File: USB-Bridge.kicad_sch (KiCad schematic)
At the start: 14 parts, among them J3 USB_B_Micro, Q4 LRC L8050QLT1G, Q5 LRC L8050QLT1G, U2 CP2102N-A02-GQFN24

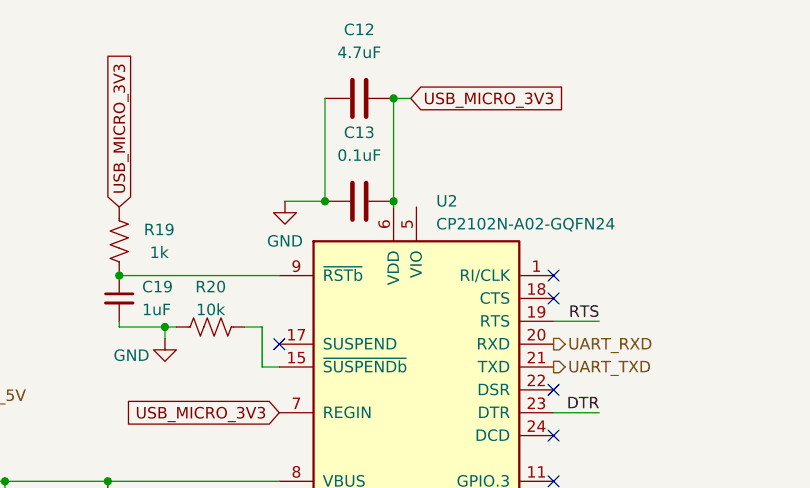
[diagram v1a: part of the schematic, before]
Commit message: added screen and gpio buttons
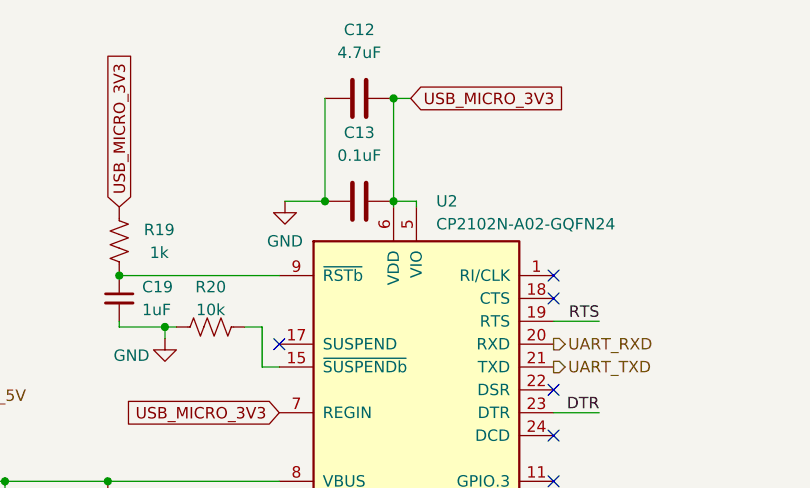
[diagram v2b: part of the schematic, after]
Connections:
- net USB_MICRO_3V3: now also U2.5 (VIO)
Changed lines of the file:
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@@
+	(wire
+		(pts
+			(xy 163.195 56.515) (xy 163.195 57.15)
+		)
+		(stroke
+			(width 0)
+			(type default)
+		)
+	)
 	(wire
 		(pts
@@
 		)
 		(stroke
+			(width 0)
+			(type default)
+		)
+	)
+	(wire
+		(pts
+			(xy 160.655 56.515) (xy 163.195 56.515)
+		)
+		(stroke

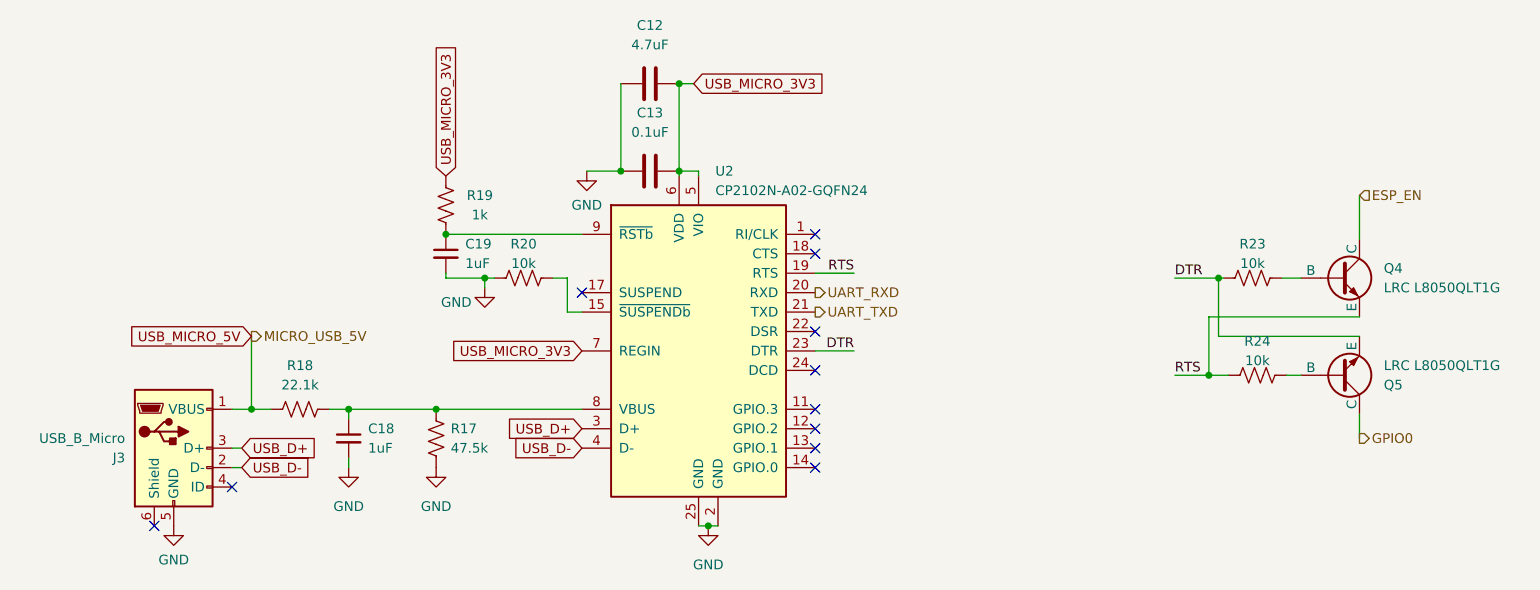
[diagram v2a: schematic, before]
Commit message: Updated current control loop hardware
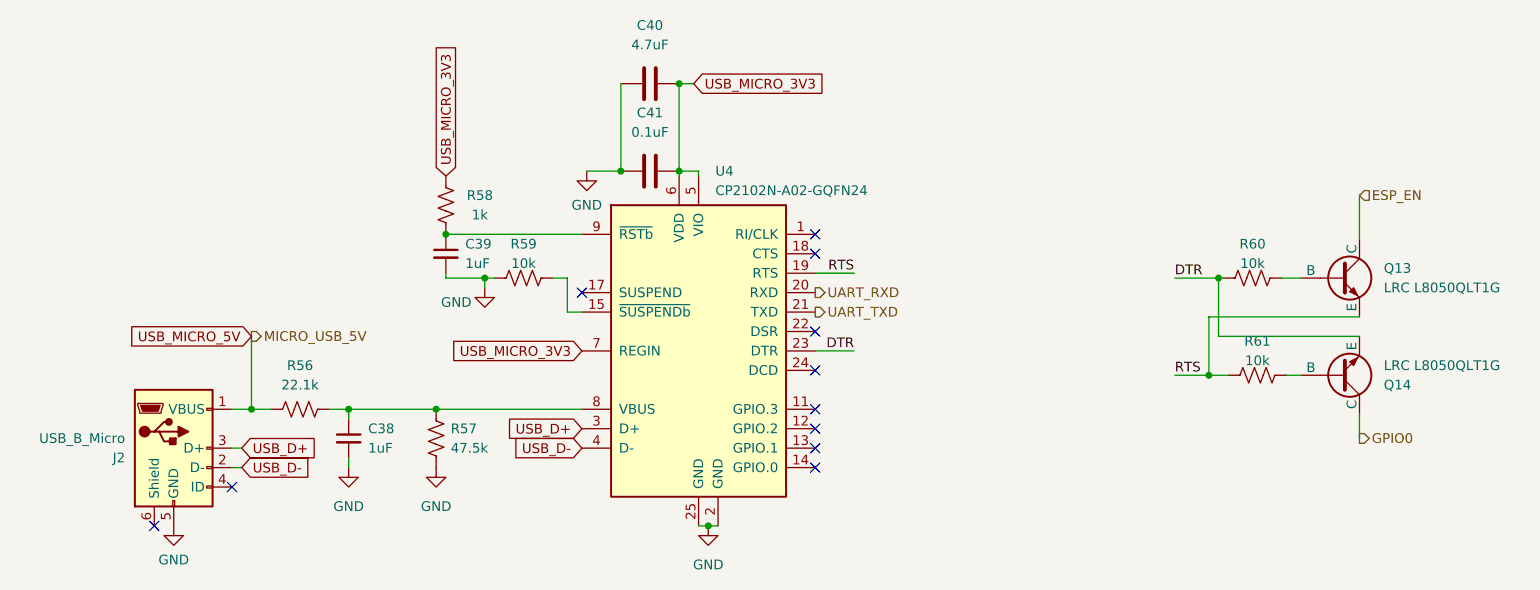
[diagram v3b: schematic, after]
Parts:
- removed C12: 4.7uF, symbol Device:C
- removed C18: 1uF, symbol Device:C_Small
- removed R17: 47.5k, symbol Device:R_US
- removed R18: 22.1k, symbol Device:R_US
- removed R19: 1k, symbol Device:R_US
- added C38: 1uF, symbol Device:C_Small
- added C40: 4.7uF, symbol Device:C
- added R56: 22.1k, symbol Device:R_US
- added R57: 47.5k, symbol Device:R_US
- added R58: 1k, symbol Device:R_US
- renumbered C19 to C39, C13 to C41, J3 to J2, Q4 to Q13, Q5 to Q14, R20 to R59, R23 to R60, R24 to R61, U2 to U4
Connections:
- net GND: now also C38.2, C40.1, R57.2
- net USB_MICRO_3V3: now also C40.2, R58.2
- net USB_MICRO_5V: now also R56.1
- net at U4.8 (VBUS): now also C38.1, R56.2, R57.1
- net at C39.1, U4.9 (~{RSTb}): now also R58.1

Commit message: All footprints assigned
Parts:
- C38, C39, C40, C41: footprint (none) -> Capacitor_SMD:C_0805_2012Metric
- Q13, Q14: footprint (none) -> Package_TO_SOT_SMD:SOT-23
- R56, R57, R58, R59, R60, R61: footprint (none) -> Resistor_SMD:R_0805_2012Metric

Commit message: updated symbol for screen and added testpoints
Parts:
- added TP16: USB_3V3, UTSVT_Special:TestPoint_HEX_3mmID, symbol Connector:TestPoint
- added TP17: uUSB_VBUS, UTSVT_Special:TestPoint_HEX_3mmID, symbol Connector:TestPoint
- added TP18: uUSB_GND, UTSVT_Special:TestPoint_HEX_3mmID, symbol Connector:TestPoint
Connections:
- net GND: now also TP18.1
- net USB_MICRO_3V3: now also TP16.1
- net at C38.1, R56.2, R57.1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: now also TP17.1
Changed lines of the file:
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@@
+	)
+	(junction
+		(at 121.92 87.63)
+		(diameter 0)
+		(color 0 0 0 0)
+	)
+	(junction
+		(at 165.735 102.87)
+		(diameter 0)
+		(color 0 0 0 0)
 	)
 	(junction
@@
 	)
 	(junction
+		(at 160.655 50.8)
+		(diameter 0)
+		(color 0 0 0 0)
+	)
+	(junction
 		(at 130.175 64.77)
 		(diameter 0)
@@
 	(wire
 		(pts
+			(xy 121.92 87.63) (xy 128.905 87.63)
+		)
+		(stroke
+			(width 0)
+			(type default)
+		)
+	)
+	(wire
+		(pts
 			(xy 231.14 78.105) (xy 249.555 78.105)
 		)
@@
 	(wire
 		(pts
-			(xy 117.475 87.63) (xy 128.905 87.63)
+			(xy 117.475 87.63) (xy 121.92 87.63)
 		)
 		(stroke
@@
 	(wire
 		(pts
-			(xy 160.655 45.085) (xy 160.655 56.515)
+			(xy 160.655 45.085) (xy 160.655 50.8)
 		)
 		(stroke
@@
 		(pts
 			(xy 130.175 64.77) (xy 147.955 64.77)
+		)
+		(stroke
+			(width 0)
+			(type default)
+		)
+	)
+	(wire
+		(pts
+			(xy 160.655 50.8) (xy 160.655 56.515)
 		)
 		(stroke
@@
 	(label "DTR"
 		(at 183.515 80.01 180)
-		(fields_autoplaced yes)
 		(effects
 			(font
@@
 	(label "DTR"
 		(at 225.425 70.485 0)
-		(fields_autoplaced yes)
 		(effects
 			(font
@@
 	(label "RTS"
 		(at 183.515 69.85 180)
-		(fields_autoplaced yes)
 		(effects
 			(font
@@
 	(label "RTS"
 		(at 225.425 83.185 0)
-		(fields_autoplaced yes)
 		(effects
 			(font
@@
 		(shape output)
 		(at 178.435 72.39 0)
-		(fields_autoplaced yes)
 		(effects
 			(font
@@
 		(shape output)
 		(at 178.435 74.93 0)
-		(fields_autoplaced yes)
 		(effects
 			(font
@@
 		(shape input)
 		(at 249.555 59.69 0)
-		(fields_autoplaced yes)
 		(effects
 			(font
@@
 		(shape output)
 		(at 249.555 91.44 0)
-		(fields_autoplaced yes)
 		(effects
 			(font
@@
 		(shape output)
 		(at 104.775 78.105 0)
-		(fields_autoplaced yes)
 		(effects
 			(font
@@
 	)
 	(symbol
+		(lib_id "Connector:TestPoint")
+		(at 121.92 87.63 0)
+		(unit 1)
+		(exclude_from_sim no)
+		(in_bom yes)
+		(on_board yes)
+		(dnp no)
+		(fields_autoplaced yes)
+		(property "Reference" "TP17"
+			(at 124.46 83.0579 0)
+			(effects
+				(font
+					(size 1.27 1.27)
+				)
+				(justify left)
+			)
+		)
+		(property "Value" "uUSB_VBUS"
+			(at 124.46 85.5979 0)
+			(effects
+				(font
+					(size 1.27 1.27)
+				)
+				(justify left)
+			)
+		)
+		(property "Footprint" "UTSVT_Special:TestPoint_HEX_3mmID"
+			(at 127 87.63 0)
+			(effects
+				(font
+					(size 1.27 1.27)
+				)
+				(hide yes)
+			)
+		)
+		(property "Datasheet" "~"
+			(at 127 87.63 0)
+			(effects
+				(font
+					(size 1.27 1.27)
+				)
+				(hide yes)
+			)
+		)
+		(property "Description" "test point"
+			(at 121.92 87.63 0)
+			(effects
+				(font
+					(size 1.27 1.27)
+				)
+				(hide yes)
+			)
+		)
+		(pin "1"
+		)
+		(instances
+			(project "Cell-Characterization-Board"
+				(path "/8cf78a1b-eb7a-4166-aa75-ad898a030304/0ac0e4f4-94aa-45a6-a3fd-2023984057ee"
+					(reference "TP17")
+					(unit 1)
+				)
+			)
+		)
+	)
+	(symbol
 		(lib_id "Device:R_US")
 		(at 140.335 70.485 270)
@@
 	)
 	(symbol
+		(lib_id "Connector:TestPoint")
+		(at 165.735 102.87 270)
+		(unit 1)
+		(exclude_from_sim no)
+		(in_bom yes)
+		(on_board yes)
+		(dnp no)
+		(fields_autoplaced yes)
+		(property "Reference" "TP18"
+			(at 170.815 101.5999 90)
+			(effects
+				(font
+					(size 1.27 1.27)
+				)
+				(justify left)
+			)
+		)
+		(property "Value" "uUSB_GND"
+			(at 170.815 104.1399 90)
+			(effects
+				(font
+					(size 1.27 1.27)
+				)
+				(justify left)
+			)
+		)
+		(property "Footprint" "UTSVT_Special:TestPoint_HEX_3mmID"
+			(at 165.735 107.95 0)
+			(effects
+				(font
+					(size 1.27 1.27)
+				)
+				(hide yes)
+			)
+		)
+		(property "Datasheet" "~"
+			(at 165.735 107.95 0)
+			(effects
+				(font
+					(size 1.27 1.27)
+				)
+				(hide yes)
+			)
+		)
+		(property "Description" "test point"
+			(at 165.735 102.87 0)
+			(effects
+				(font
+					(size 1.27 1.27)
+				)
+				(hide yes)
+			)
+		)
+		(pin "1"
+		)
+		(instances
+			(project "Cell-Characterization-Board"
+				(path "/8cf78a1b-eb7a-4166-aa75-ad898a030304/0ac0e4f4-94aa-45a6-a3fd-2023984057ee"
+					(reference "TP18")
+					(unit 1)
+				)
+			)
+		)
+	)
+	(symbol
 		(lib_id "power:GND")
 		(at 135.255 71.755 0)
@@
 					(unit 1)
 				)
+			)
+		)
+	)
+	(symbol
+		(lib_id "Connector:TestPoint")
+		(at 160.655 50.8 270)
+		(unit 1)
+		(exclude_from_sim no)
+		(in_bom yes)
+		(on_board yes)
+		(dnp no)
+		(fields_autoplaced yes)
+		(property "Reference" "TP16"
+			(at 165.735 49.5299 90)
+			(effects
+				(font
+					(size 1.27 1.27)
+				)
+				(justify left)
+			)
+		)
+		(property "Value" "USB_3V3"
+			(at 165.735 52.0699 90)
+			(effects
+				(font
+					(size 1.27 1.27)
+				)
+				(justify left)
+			)
+		)
+		(property "Footprint" "UTSVT_Special:TestPoint_HEX_3mmID"
+			(at 160.655 55.88 0)
+			(effects
+				(font
+					(size 1.27 1.27)
+				)
+				(hide yes)
+			)
+		)
+		(property "Datasheet" "~"
+			(at 160.655 55.88 0)
+			(effects
+				(font
+					(size 1.27 1.27)
+				)
+				(hide yes)
+			)
+		)
+		(property "Description" "test point"
+			(at 160.655 50.8 0)
+			(effects
+				(font
+					(size 1.27 1.27)
+				)
+				(hide yes)
+			)
+		)
+		(pin "1"
+		)
+		(instances
+			(project "Cell-Characterization-Board"
+				(path "/8cf78a1b-eb7a-4166-aa75-ad898a030304/0ac0e4f4-94aa-45a6-a3fd-2023984057ee"
+					(reference "TP16")
+					(unit 1)
+				)
